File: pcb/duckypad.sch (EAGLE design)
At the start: 137 parts, among them IC2 REG1117, SW1 SPST_TACT-EVQQ2, SW2 SPST_TACT-EVQQ2, SW21 EC12E_SW, SW22 EC12E_SW, SW3 324_SW324_SWITCH_FOOT_HOLE, U1 USBC_16P, U2 USBC_16P, U3 ESP32-S3FN8, Y1 16MHz_12pF

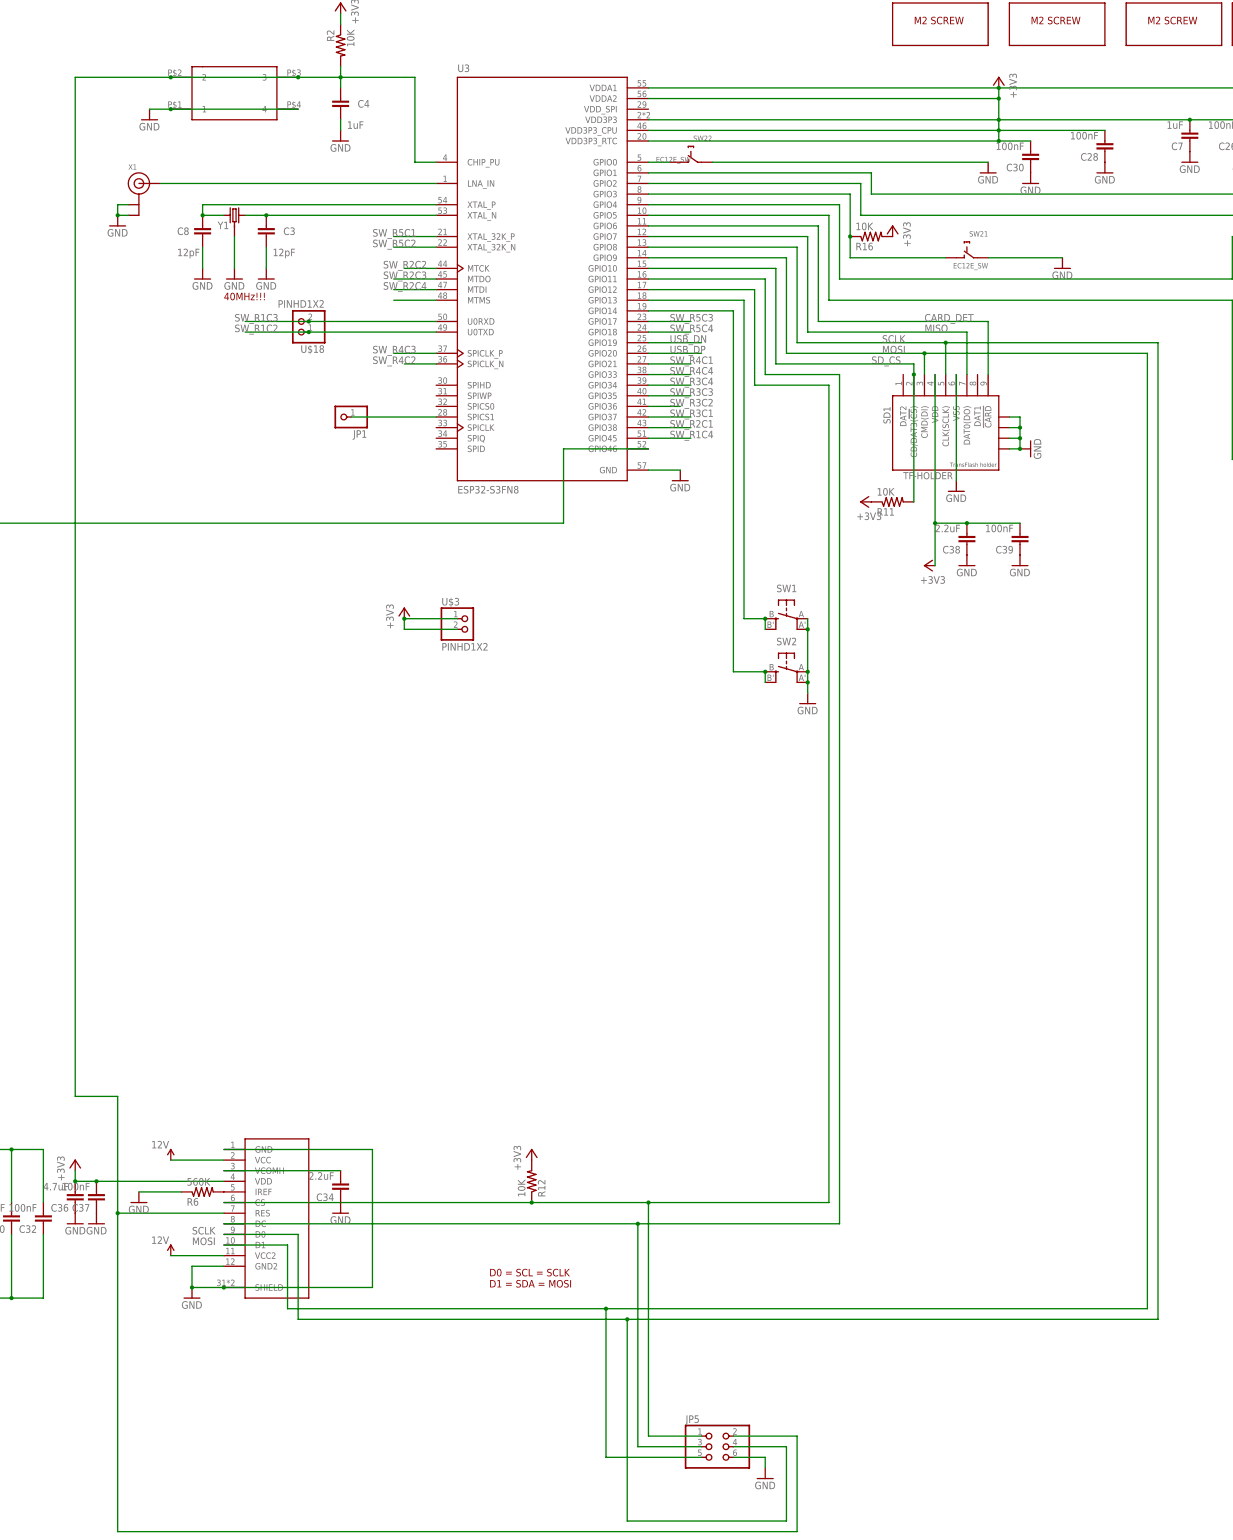
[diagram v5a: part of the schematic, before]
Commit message: updating pcb
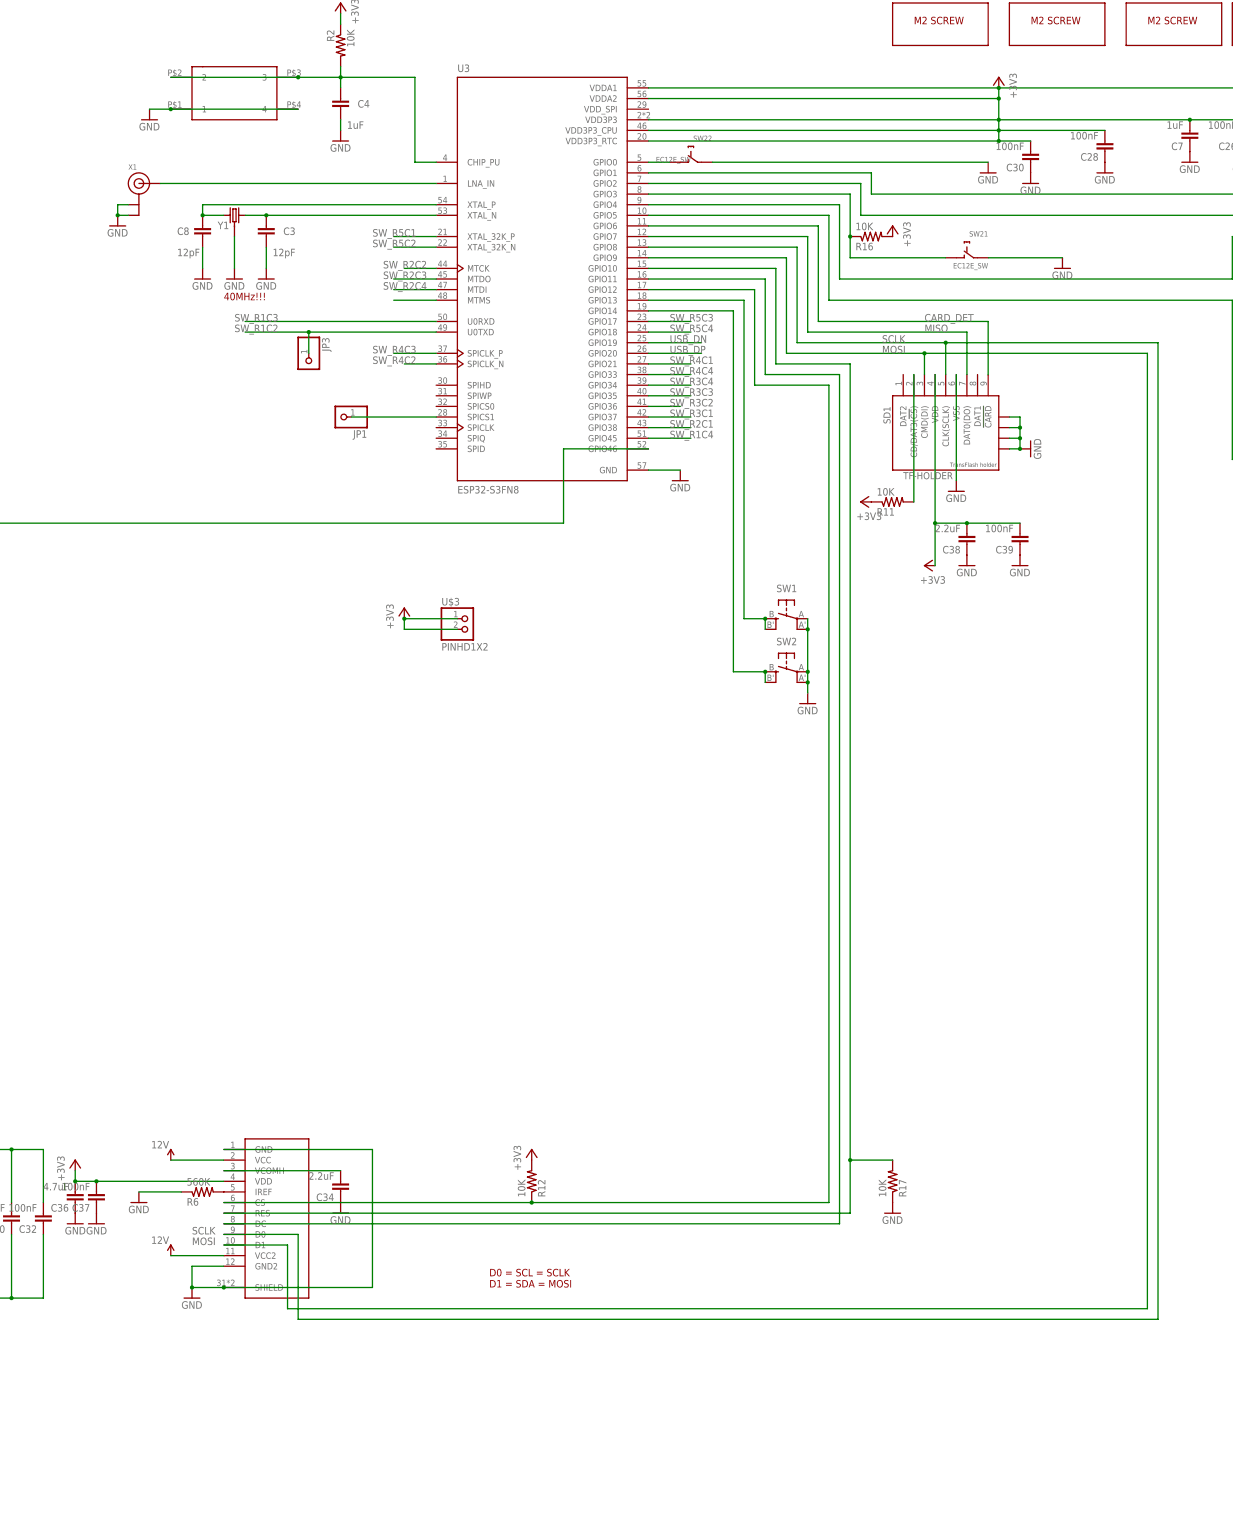
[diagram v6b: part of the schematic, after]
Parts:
- removed JP5: (no value), pinhead:PINHD-2X3
- removed U$18: PINHD1X2, adafruit_changed:PINHD1X2
- added JP3: (no value), adafruit_changed:PINHD-1X1CB
- added R17: 10K, joyAnalog:RESISTOR0805-RES
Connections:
- removed net RESET: C4.1, JP5.2, R2.2, SW3.2, SW3.3, U$2.RES, U3.CHIP_PU
- removed net SD_CS: R11.2, SD1.CD/DAT3(!CS!), U3.GPIO10
- new net N$43: R11.2, SD1.CD/DAT3(!CS!)
- new net N$45: C4.1, R2.2, SW3.2, SW3.3, U3.CHIP_PU
- new net OLED_RESET: R17.2, U$2.RES, U3.GPIO10
- net DC: no longer JP5.3
- net GND: now also R17.1; no longer JP5.6
- net MOSI: no longer JP5.5
- net OLED_CS: no longer JP5.1
- net SCLK: no longer JP5.4
- net SW_R1C2: now also JP3.1; no longer U$18.1
- net SW_R1C3: no longer U$18.2

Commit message: moving pins around
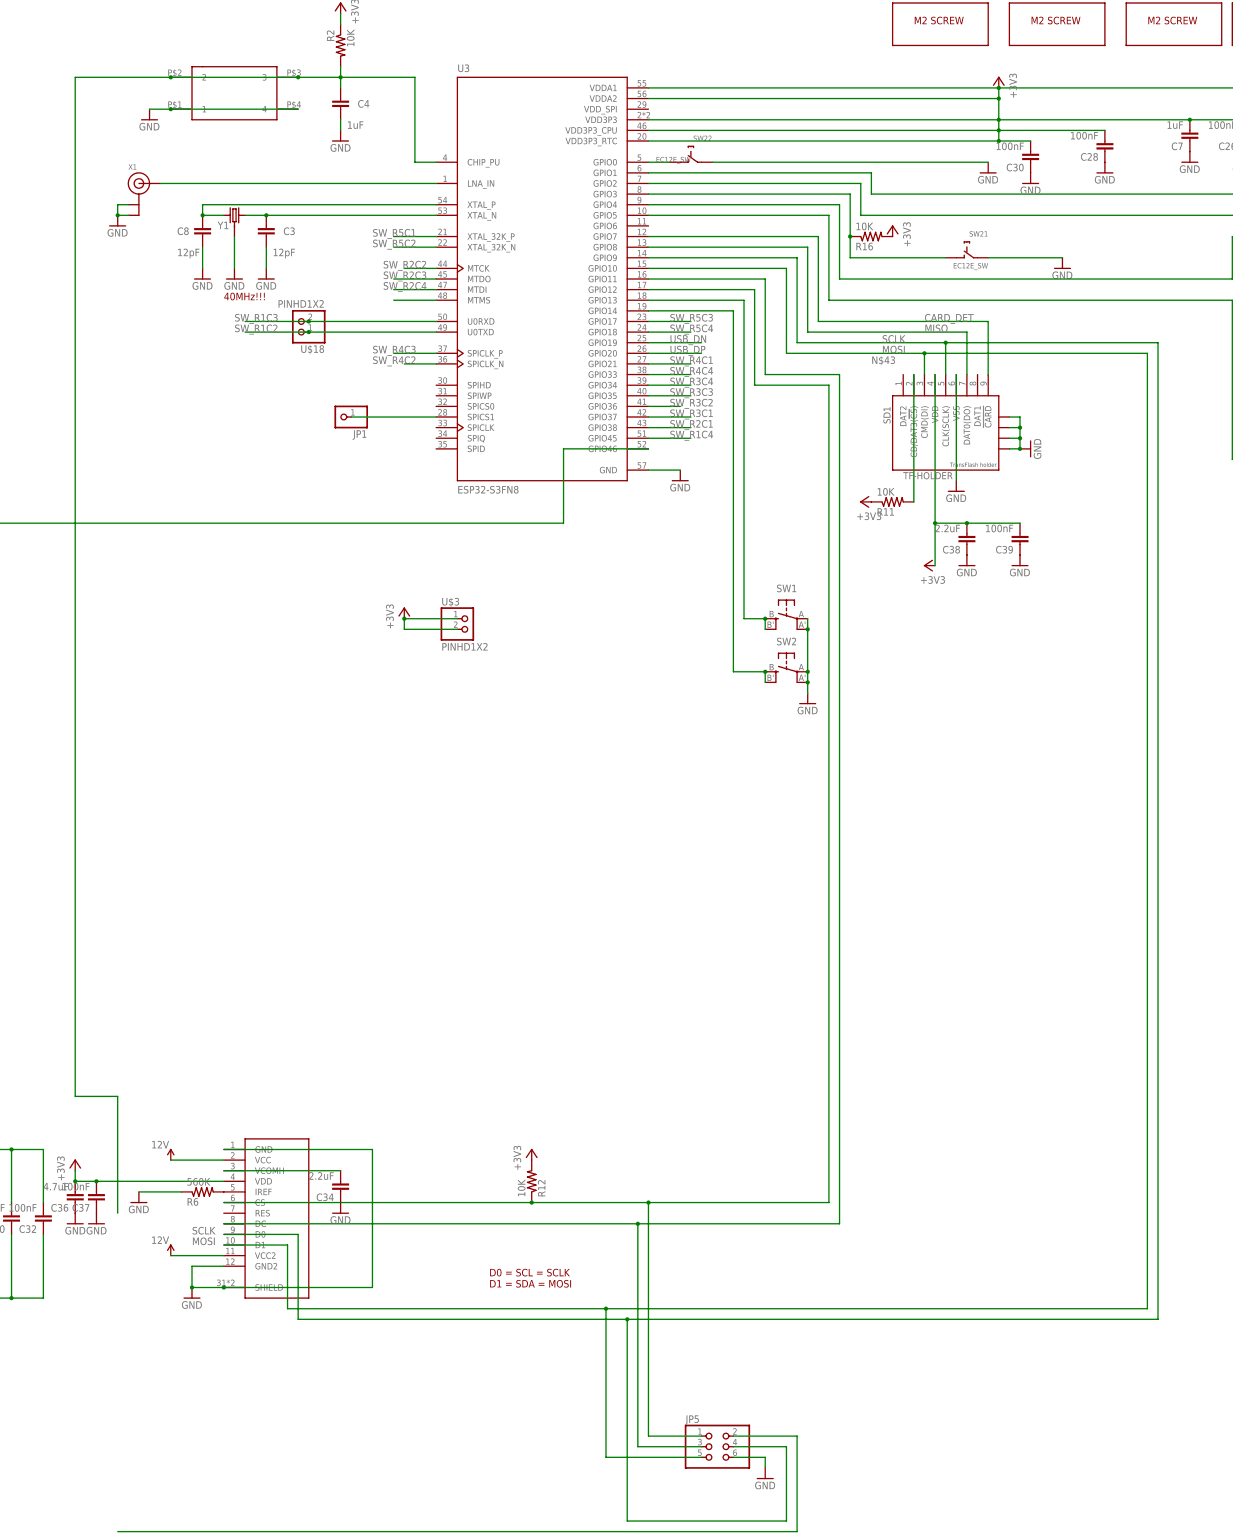
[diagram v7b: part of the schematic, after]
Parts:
- removed JP3: (no value), adafruit_changed:PINHD-1X1CB
- removed R17: 10K, joyAnalog:RESISTOR0805-RES
- added JP5: (no value), pinhead:PINHD-2X3
- added U$18: PINHD1X2, adafruit_changed:PINHD1X2
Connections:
- net N$45 renamed RESET
- removed net OLED_RESET: R17.2, U$2.RES, U3.GPIO10
- new net N$44: JP5.2
- net CARD_DET: now also U3.GPIO7; no longer U3.GPIO6
- net DC: now also JP5.3
- net GND: now also JP5.6; no longer R17.1
- net MISO: now also U3.GPIO8; no longer U3.GPIO7
- net MOSI: now also JP5.5, U3.GPIO10; no longer U3.GPIO9
- net OLED_CS: now also JP5.1
- net SCLK: now also JP5.4, U3.GPIO9; no longer U3.GPIO8
- net SW_R1C2: now also U$18.1; no longer JP3.1
- net SW_R1C3: now also U$18.2

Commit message: updated PCB
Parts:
- removed U$18: PINHD1X2, adafruit_changed:PINHD1X2
- added JP3: (no value), adafruit_changed:PINHD-1X1CB
- added R17: 10K, joyAnalog:RESISTOR0805-RES
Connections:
- removed net N$44: JP5.2
- new net OLED_RESET: JP5.2, R17.2, U$2.RES, U3.GPIO6
- net GND: now also R17.1
- net SW_R1C2: now also JP3.1; no longer U$18.1
- net SW_R1C3: no longer U$18.2
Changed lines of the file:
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@@
 <part name="R3" library="joyAnalog" deviceset="RESISTOR" device="0805-RES" value="5.1K"/>
 <part name="R4" library="joyAnalog" deviceset="RESISTOR" device="0805-RES" value="5.1K"/>
-<part name="U$18" library="adafruit_changed" deviceset="PINHD1X2" device=""/>
 <part name="C5" library="clock" deviceset="CAP" device="0805" value="1uF"/>
 <part name="C6" library="clock" deviceset="CAP" device="0805" value="100nF"/>
@@
 <part name="D2" library="Discrete_NOA" library_urn="urn:adsk.eagle:library:2000212" deviceset="D*" device="214AA" package3d_urn="urn:adsk.eagle:package:2068475/4" value="SS14"/>
 <part name="C46" library="clock" deviceset="CAP" device="0805" value="100nF"/>
+<part name="R17" library="joyAnalog" deviceset="RESISTOR" device="0805-RES" value="10K"/>
+<part name="GND62" library="supply1" library_urn="urn:adsk.eagle:library:371" deviceset="GND" device=""/>
+<part name="JP3" library="adafruit_changed" deviceset="PINHD-1X1" device="CB"/>
 </parts>
 <sheets>
@@
 <attribute name="VALUE" x="-1.27" y="-186.182" size="1.778" layer="96" rot="MR0"/>
 </instance>
-<instance part="U$18" gate="1" x="314.96" y="-68.58" smashed="yes" rot="R180">
-<attribute name="NAME" x="321.31" y="-74.295" size="1.778" layer="95" rot="R180"/>
-<attribute name="VALUE" x="321.31" y="-63.5" size="1.778" layer="96" rot="R180"/>
-</instance>
 <instance part="C5" gate="G$1" x="551.18" y="-15.24" smashed="yes" rot="R180">
 <attribute name="NAME" x="549.656" y="-18.161" size="1.778" layer="95" rot="R180"/>
@@
 <attribute name="NAME" x="232.156" y="-284.861" size="1.778" layer="95" rot="R180"/>
 <attribute name="VALUE" x="232.156" y="-279.781" size="1.778" layer="96" rot="R180"/>
+</instance>
+<instance part="R17" gate="G$1" x="477.52" y="-287.02" smashed="yes" rot="MR90">
+<attribute name="NAME" x="479.0186" y="-290.83" size="1.778" layer="95" rot="MR90"/>
+<attribute name="VALUE" x="474.218" y="-290.83" size="1.778" layer="96" rot="MR90"/>
+<attribute name="NAME" x="479.0186" y="-290.83" size="1.778" layer="95" rot="MR90"/>
+<attribute name="VALUE" x="474.218" y="-290.83" size="1.778" layer="96" rot="MR90"/>
+</instance>
+<instance part="GND62" gate="1" x="477.52" y="-294.64" smashed="yes">
+<attribute name="VALUE" x="474.98" y="-297.18" size="1.778" layer="96"/>
+</instance>
+<instance part="JP3" gate="G$1" x="320.04" y="-78.74" smashed="yes" rot="R270">
+<attribute name="NAME" x="323.215" y="-72.39" size="1.778" layer="95" rot="R270"/>
+<attribute name="VALUE" x="314.96" y="-72.39" size="1.778" layer="96" rot="R270"/>
 </instance>
 </instances>
@@
 <wire x1="426.72" y1="-340.36" x2="426.72" y2="-342.9" width="0.1524" layer="91"/>
 </segment>
+<segment>
+<pinref part="R17" gate="G$1" pin="1"/>
+<pinref part="GND62" gate="1" pin="GND"/>
+</segment>
 </net>
 <net name="+3V3" class="0">
@@
 <segment>
 <pinref part="U3" gate="G$1" pin="U0TXD"/>
-<pinref part="U$18" gate="1" pin="1"/>
-<wire x1="347.98" y1="-71.12" x2="317.5" y2="-71.12" width="0.1524" layer="91"/>
-<wire x1="302.26" y1="-71.12" x2="317.5" y2="-71.12" width="0.1524" layer="91"/>
-<junction x="317.5" y="-71.12"/>
+<wire x1="347.98" y1="-71.12" x2="320.04" y2="-71.12" width="0.1524" layer="91"/>
 <label x="299.72" y="-71.12" size="1.778" layer="95"/>
+<pinref part="JP3" gate="G$1" pin="1"/>
+<wire x1="320.04" y1="-71.12" x2="302.26" y2="-71.12" width="0.1524" layer="91"/>
+<wire x1="320.04" y1="-76.2" x2="320.04" y2="-71.12" width="0.1524" layer="91"/>
+<junction x="320.04" y="-71.12"/>
 </segment>
 </net>
@@
 </segment>
 <segment>
-<wire x1="317.5" y1="-68.58" x2="302.26" y2="-68.58" width="0.1524" layer="91"/>
 <pinref part="U3" gate="G$1" pin="U0RXD"/>
-<pinref part="U$18" gate="1" pin="2"/>
-<wire x1="347.98" y1="-68.58" x2="317.5" y2="-68.58" width="0.1524" layer="91"/>
-<junction x="317.5" y="-68.58"/>
+<wire x1="347.98" y1="-68.58" x2="302.26" y2="-68.58" width="0.1524" layer="91"/>
 <label x="299.72" y="-68.58" size="1.778" layer="95"/>
 </segment>
@@
 <net name="RESET" class="0">
 <segment>
-<wire x1="271.78" y1="-281.94" x2="271.78" y2="-254" width="0.1524" layer="91"/>
 <pinref part="SW3" gate="G$1" pin="2"/>
 <pinref part="SW3" gate="G$1" pin="3"/>
@@
 <wire x1="314.96" y1="-10.16" x2="325.12" y2="-10.16" width="0.1524" layer="91"/>
 <junction x="314.96" y="-10.16"/>
-<wire x1="284.48" y1="-10.16" x2="261.62" y2="-10.16" width="0.1524" layer="91"/>
-<junction x="284.48" y="-10.16"/>
-<wire x1="261.62" y1="-10.16" x2="261.62" y2="-254" width="0.1524" layer="91"/>
-<wire x1="271.78" y1="-254" x2="261.62" y2="-254" width="0.1524" layer="91"/>
 </segment>
 </net>
@@
 <net name="CARD_DET" class="0">
 <segment>
-<wire x1="439.42" y1="-48.26" x2="439.42" y2="-68.58" width="0.1524" layer="91"/>
-<wire x1="439.42" y1="-68.58" x2="480.06" y2="-68.58" width="0.1524" layer="91"/>
+<wire x1="436.88" y1="-48.26" x2="436.88" y2="-68.58" width="0.1524" layer="91"/>
+<wire x1="436.88" y1="-68.58" x2="480.06" y2="-68.58" width="0.1524" layer="91"/>
 <wire x1="480.06" y1="-68.58" x2="480.06" y2="-81.28" width="0.1524" layer="91"/>
 <pinref part="SD1" gate="G$1" pin="!CARD"/>
 <label x="464.82" y="-68.58" size="1.778" layer="95"/>
 <pinref part="U3" gate="G$1" pin="GPIO7"/>
-<wire x1="398.78" y1="-48.26" x2="439.42" y2="-48.26" width="0.1524" layer="91"/>
+<wire x1="398.78" y1="-48.26" x2="436.88" y2="-48.26" width="0.1524" layer="91"/>
 </segment>
 </net>
 <net name="MISO" class="0">
 <segment>
-<wire x1="436.88" y1="-50.8" x2="436.88" y2="-71.12" width="0.1524" layer="91"/>
-<wire x1="436.88" y1="-71.12" x2="474.98" y2="-71.12" width="0.1524" layer="91"/>
+<wire x1="434.34" y1="-50.8" x2="434.34" y2="-71.12" width="0.1524" layer="91"/>
+<wire x1="434.34" y1="-71.12" x2="474.98" y2="-71.12" width="0.1524" layer="91"/>
 <pinref part="SD1" gate="G$1" pin="DAT0(DO)"/>
 <wire x1="474.98" y1="-71.12" x2="474.98" y2="-81.28" width="0.1524" layer="91"/>
 <label x="464.82" y="-71.12" size="1.778" layer="95"/>
 <pinref part="U3" gate="G$1" pin="GPIO8"/>
-<wire x1="398.78" y1="-50.8" x2="436.88" y2="-50.8" width="0.1524" layer="91"/>
+<wire x1="398.78" y1="-50.8" x2="434.34" y2="-50.8" width="0.1524" layer="91"/>
 </segment>
 </net>
@@
 <pinref part="SD1" gate="G$1" pin="CLK(SCLK)"/>
 <wire x1="469.9" y1="-81.28" x2="469.9" y2="-73.66" width="0.1524" layer="91"/>
-<wire x1="469.9" y1="-73.66" x2="434.34" y2="-73.66" width="0.1524" layer="91"/>
-<wire x1="434.34" y1="-73.66" x2="434.34" y2="-53.34" width="0.1524" layer="91"/>
+<wire x1="469.9" y1="-73.66" x2="431.8" y2="-73.66" width="0.1524" layer="91"/>
+<wire x1="431.8" y1="-73.66" x2="431.8" y2="-53.34" width="0.1524" layer="91"/>
 <label x="454.66" y="-73.66" size="1.778" layer="95"/>
 <pinref part="U$2" gate="G$1" pin="D0"/>
@@
 <wire x1="431.8" y1="-337.82" x2="419.1" y2="-337.82" width="0.1524" layer="91"/>
 <pinref part="U3" gate="G$1" pin="GPIO9"/>
-<wire x1="398.78" y1="-53.34" x2="434.34" y2="-53.34" width="0.1524" layer="91"/>
+<wire x1="398.78" y1="-53.34" x2="431.8" y2="-53.34" width="0.1524" layer="91"/>
 </segment>
 </net>
@@
 <pinref part="SD1" gate="G$1" pin="CMD(DI)"/>
 <wire x1="464.82" y1="-81.28" x2="464.82" y2="-76.2" width="0.1524" layer="91"/>
-<wire x1="464.82" y1="-76.2" x2="431.8" y2="-76.2" width="0.1524" layer="91"/>
-<wire x1="431.8" y1="-76.2" x2="431.8" y2="-55.88" width="0.1524" layer="91"/>
+<wire x1="464.82" y1="-76.2" x2="429.26" y2="-76.2" width="0.1524" layer="91"/>
+<wire x1="429.26" y1="-76.2" x2="429.26" y2="-55.88" width="0.1524" layer="91"/>
 <label x="454.66" y="-76.2" size="1.778" layer="95"/>
 <pinref part="U$2" gate="G$1" pin="D1"/>
@@
 <junction x="388.62" y="-304.8"/>
 <pinref part="U3" gate="G$1" pin="GPIO10"/>
-<wire x1="398.78" y1="-55.88" x2="431.8" y2="-55.88" width="0.1524" layer="91"/>
+<wire x1="398.78" y1="-55.88" x2="429.26" y2="-55.88" width="0.1524" layer="91"/>
 </segment>
 </net>
@@
 </segment>
 </net>
-<net name="N$44" class="0">
+<net name="OLED_RESET" class="0">
 <segment>
 <pinref part="JP5" gate="A" pin="2"/>
 <wire x1="434.34" y1="-335.28" x2="419.1" y2="-335.28" width="0.1524" layer="91"/>
-<wire x1="271.78" y1="-358.14" x2="434.34" y2="-358.14" width="0.1524" layer="91"/>
-<wire x1="434.34" y1="-358.14" x2="434.34" y2="-335.28" width="0.1524" layer="91"/>
-</segment>
-</net>
+<pinref part="U3" gate="G$1" pin="GPIO6"/>
+<wire x1="398.78" y1="-45.72" x2="439.42" y2="-45.72" width="0.1524" layer="91"/>
+<wire x1="439.42" y1="-45.72" x2="439.42" y2="-66.04" width="0.1524" layer="91"/>
+<wire x1="439.42" y1="-66.04" x2="525.78" y2="-66.04" width="0.1524" layer="91"/>
+<pinref part="U$2" gate="G$1" pin="RES"/>
+<wire x1="525.78" y1="-66.04" x2="525.78" y2="-281.94" width="0.1524" layer="91"/>
+<wire x1="525.78" y1="-281.94" x2="477.52" y2="-281.94" width="0.1524" layer="91"/>
+<pinref part="R17" gate="G$1" pin="2"/>
+<wire x1="477.52" y1="-281.94" x2="434.34" y2="-281.94" width="0.1524" layer="91"/>
+<junction x="477.52" y="-281.94"/>
+<wire x1="434.34" y1="-281.94" x2="297.18" y2="-281.94" width="0.1524" layer="91"/>
+<wire x1="434.34" y1="-335.28" x2="434.34" y2="-281.94" width="0.1524" layer="91"/>
+<junction x="434.34" y="-281.94"/>
+</segment>
+</net>
